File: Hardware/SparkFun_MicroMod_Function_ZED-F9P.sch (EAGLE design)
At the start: 107 parts, among them J1 USB Female Type C Connector, J10 U.FL, J11 455-1750-1-ND, J15 QWIIC_RA, J16 QWIIC_RA, J18 Bus Selection, J2 MICROMOD_STANDARD, J3 Bus Selection, Q1 DMP21D0UT, U1 SN74LVC1G66DRYR, U10 SN74AUP1T04DCK, U11 SN74AUP1T04DCK, U2 3.3V, U3 EEPROM, U4 74LVC4066D_QUAD_BILATERAL_SWI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, U5 74LVC4066D_QUAD_BILATERAL_SWI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, U6 OPA344, U7 74LVC541ABQ, U8 U-BLOX_ZED-F9P, U9 FIN1017MXSOIC-8

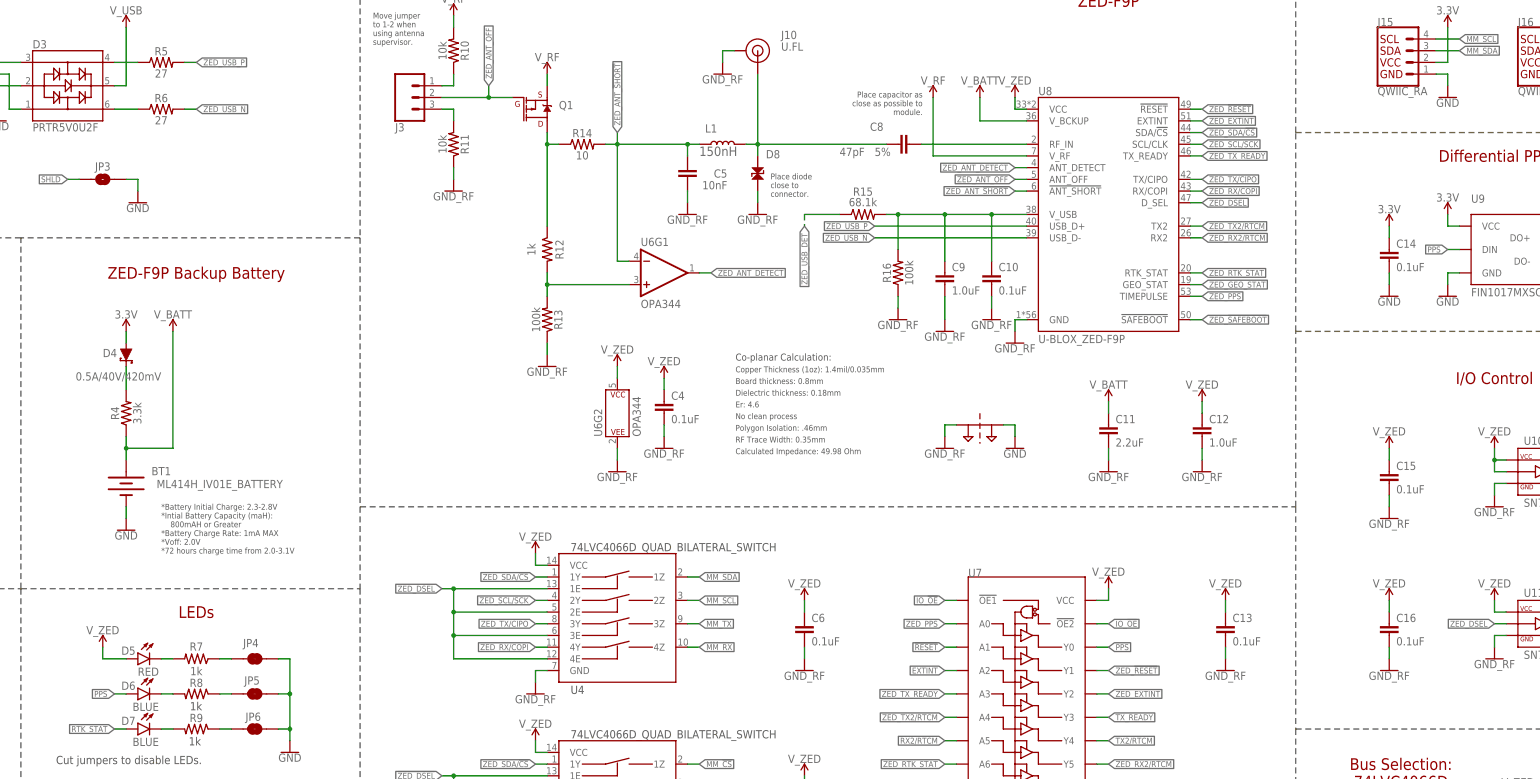
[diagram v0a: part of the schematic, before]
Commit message: Everything tentatively placed on board.
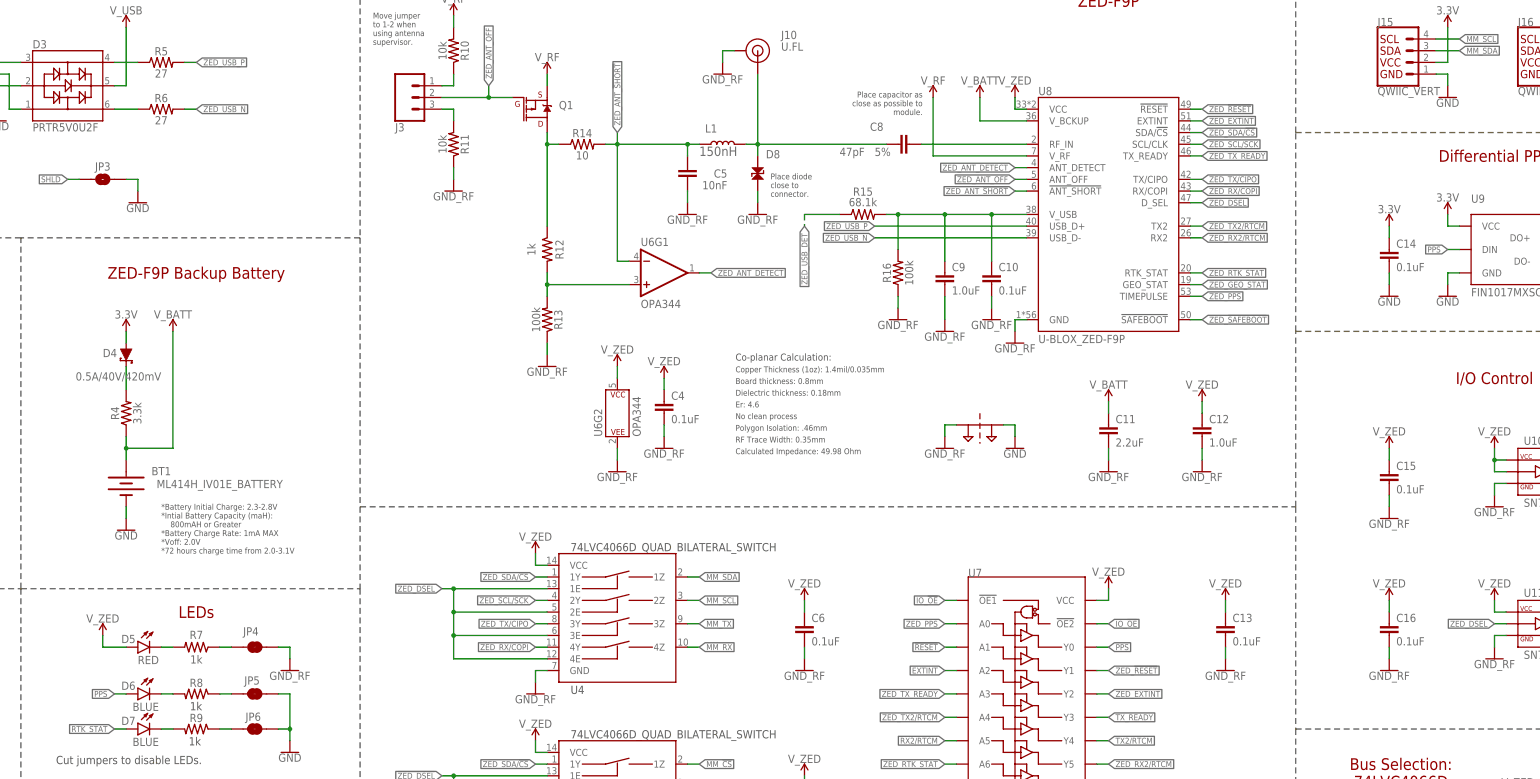
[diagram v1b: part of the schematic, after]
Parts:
- J15: value QWIIC_RA -> QWIIC_VERT; device SparkFun-Connectors:QWIIC_CONNECTORJS-1MM -> SparkFun-Connectors:QWIIC_CONNECTOR
- J7: device SparkFun-Connectors:CONN_01 -> SparkFun-Connectors:CONN_01PTH_NO_SILK_SMALL
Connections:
- net GND: no longer JP4.2
- net GND_RF: now also JP4.2
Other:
- moved on the sheet: D5, JP4, R7

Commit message: 1st draft power planes.
Added split power planes to layout on inner layers.
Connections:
- net N$51 renamed PPS_DIFF_N
- net N$9 renamed PPS_DIFF_P
- net GND: no longer U1.VSS
- net GND_RF: now also U1.VSS

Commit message: Board updates from time off.
Airport board layout was time well spent.
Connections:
- net N$1 renamed USBC_P
- net N$2 renamed USBC_N
- net N$5 renamed USB_P
- net N$6 renamed USB_N
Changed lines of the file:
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@@
 <clearance class="1" value="0.64"/>
 <clearance class="2" value="0.46"/>
+<clearance class="3" value="0.1"/>
 </class>
-<class number="4" name="3.3V" width="0" drill="0">
+<class number="4" name="3.3V" width="0.2" drill="0">
+<clearance class="1" value="0.2"/>
 </class>
 <class number="5" name="5V" width="0" drill="0">
+<clearance class="1" value="0.2"/>
 <clearance class="4" value="0.1"/>
 </class>
-<class number="6" name="USB_DIFF" width="0" drill="0">
+<class number="6" name="USB_DIFF" width="0.2" drill="0">
 </class>
 <class number="7" name="V_ZED" width="0" drill="0">
+<clearance class="1" value="0.2"/>
+<clearance class="2" value="0.2"/>
 <clearance class="4" value="0.64"/>
 </class>
-<class number="8" name="V_RF" width="0.35" drill="0">
+<class number="8" name="V_RF" width="0.2" drill="0">
 <clearance class="2" value="0.46"/>
 </class>
-<class number="9" name="PPS_DIFF" width="0" drill="0">
+<class number="9" name="PPS_DIFF" width="0.2" drill="0">
 </class>
-<class number="10" name="DIGITAL" width="0" drill="0">
+<class number="10" name="DIGITAL" width="0.09" drill="0">
+<clearance class="0" value="0.1"/>
+<clearance class="1" value="0.1"/>
+<clearance class="10" value="0.1"/>
 </class>
-<class number="11" name="ZED_DIG" width="0" drill="0">
+<class number="11" name="ZED_DIG" width="0.1" drill="0">
+<clearance class="0" value="0.2"/>
+<clearance class="1" value="0.2"/>
+<clearance class="2" value="0.2"/>
+<clearance class="3" value="0.46"/>
+<clearance class="7" value="0.1"/>
+<clearance class="11" value="0.1"/>
 </class>
 </classes>
@@
 </segment>
 </net>
-<net name="N$1" class="0">
+<net name="USBC_P" class="6">
 <segment>
 <wire x1="40.64" y1="248.92" x2="73.66" y2="248.92" width="0.1524" layer="91"/>
@@
 </segment>
 </net>
-<net name="N$2" class="0">
+<net name="USBC_N" class="6">
 <segment>
 <wire x1="40.64" y1="246.38" x2="71.12" y2="246.38" width="0.1524" layer="91"/>
@@
 </segment>
 </net>
-<net name="N$5" class="0">
+<net name="USB_P" class="6">
 <segment>
 <pinref part="R5" gate="G$1" pin="1"/>
@@
 </segment>
 </net>
-<net name="N$6" class="0">
+<net name="USB_N" class="6">
 <segment>
 <pinref part="R6" gate="G$1" pin="1"/>
@@
 </segment>
 </net>
-<net name="N$14" class="5">
+<net name="N$14" class="4">
 <segment>
 <pinref part="R15" gate="&gt;NAME" pin="2"/>

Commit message: Update sch after fixing lib.
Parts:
- JP3: value JUMPER-SMT_2_NO_SILK -> JUMPER-SMT_2_NC_TRACE_SILK; device SparkFun-Jumpers:JUMPER-SMT_2_NO_SILK -> SparkFun-Jumpers:JUMPER-SMT_2_NC_TRACE_SILK
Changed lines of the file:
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@@
 </class>
 <class number="7" name="V_ZED" width="0" drill="0">
-<clearance class="1" value="0.2"/>
+<clearance class="1" value="0.64"/>
 <clearance class="2" value="0.2"/>
 <clearance class="4" value="0.64"/>
@@
 <part name="SUPPLY28" library="SparkFun-PowerSymbols" deviceset="3.3V" device=""/>
 <part name="SUPPLY29" library="SparkFun-PowerSymbols" deviceset="3.3V" device=""/>
-<part name="JP3" library="SparkFun-Jumpers" deviceset="JUMPER-SMT_2_NO" device="_SILK" package3d_urn="urn:adsk.eagle:package:39279/1"/>
+<part name="JP3" library="SparkFun-Jumpers" deviceset="JUMPER-SMT_2_NC_TRACE" device="_SILK" package3d_urn="urn:adsk.eagle:package:39281/1"/>
 <part name="GND5" library="SparkFun-PowerSymbols" deviceset="GND" device=""/>
 <part name="JP1" library="SparkFun-Jumpers" deviceset="JUMPER-SMT_2_NO" device="_SILK" package3d_urn="urn:adsk.eagle:package:39279/1"/>

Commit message: Replace backup battery.
New part now in use.
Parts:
- BT1: value ML414H_IV01E_BATTERY -> RELOWABLE_BATTERY_MS421R; device SparkFun-Batteries:ML414H_IV01E_BATTERY -> SparkFun-Batteries:RELOWABLE_BATTERY_MS421R
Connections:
- net GEO_STAT: now also J2.F6; no longer J2.F5
- net RTK_STAT: now also J2.F5; no longer J2.F6
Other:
- note added: "*Battery Initial Charge: 2.8-3.3V *Intial Battery Capacity (maH): 1.5mAh *Battery Charge Rate: 1mA MAX *Voff: 2.0V *120 hours charge time from 2.0-3.1V"
- note removed: "*Battery Initial Charge: 2.3-2.8V *Intial Battery Capacity (maH): 800mAH or Greater *Battery Charge Rate: 1mA MAX *Voff: 2.0V *72 hours charge time from 2.0-3.1V"
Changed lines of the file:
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@@
 <part name="SUPPLY11" library="SparkFun-PowerSymbols" deviceset="3.3V" device=""/>
 <part name="D4" library="SparkFun-DiscreteSemi" deviceset="DIODE-SCHOTTKY" device="-PMEG4005EJ" value="0.5A/40V/420mV"/>
-<part name="BT1" library="SparkFun-Batteries" deviceset="ML414H_IV01E_BATTERY" device=""/>
+<part name="BT1" library="SparkFun-Batteries" deviceset="RELOWABLE_BATTERY" device="_MS421R"/>
 <part name="D6" library="SparkFun-LED" deviceset="LED-BLUE" device="0603" value="BLUE"/>
 <part name="D7" library="SparkFun-LED" deviceset="LED-BLUE" device="0603" value="BLUE"/>
@@
 <text x="228.854" y="184.15" size="1.524" layer="97" font="vector" ratio="15">Co-planar Calculation:</text>
 <text x="228.854" y="163.83" size="1.27" layer="97" font="vector">Calculated Impedance: 49.98 Ohm</text>
-<text x="104.14" y="142.24" size="1.27" layer="97" font="vector">*Battery Initial Charge: 2.3-2.8V
+<text x="104.14" y="142.24" size="1.27" layer="97" font="vector">*Battery Initial Charge: 2.8-3.3V
 *Intial Battery Capacity (maH):
-    800mAH or Greater
+    1.5mAh
 *Battery Charge Rate: 1mA MAX
 *Voff: 2.0V
-*72 hours charge time from 2.0-3.1V</text>
+*120 hours charge time from 2.0-3.1V</text>
 <text x="269.494" y="237.49" size="1.27" layer="97" font="vector" align="bottom-right">Place capacitor as
 close as possible to
@@
 <instance part="BT1" gate="G$1" x="96.52" y="157.48" smashed="yes" rot="R270">
 <attribute name="NAME" x="104.14" y="159.258" size="1.778" layer="95" font="vector" align="bottom-center"/>
-<attribute name="VALUE" x="116.84" y="158.242" size="1.778" layer="96" font="vector" align="top-center"/>
 </instance>
 <instance part="D6" gate="G$1" x="99.06" y="111.76" smashed="yes" rot="MR270">
@@
 </segment>
 <segment>
-<wire x1="116.84" y1="17.78" x2="114.3" y2="17.78" width="0.1524" layer="91"/>
-<label x="116.84" y="17.78" size="1.27" layer="95" xref="yes"/>
-<pinref part="J2" gate="J1" pin="F6"/>
+<wire x1="116.84" y1="20.32" x2="114.3" y2="20.32" width="0.1524" layer="91"/>
+<pinref part="J2" gate="J1" pin="F5"/>
+<label x="116.84" y="20.32" size="1.27" layer="95" xref="yes"/>
 </segment>
 </net>
@@
 </segment>
 <segment>
-<wire x1="116.84" y1="20.32" x2="114.3" y2="20.32" width="0.1524" layer="91"/>
-<label x="116.84" y="20.32" size="1.27" layer="95" xref="yes"/>
-<pinref part="J2" gate="J1" pin="F5"/>
-</segment>
-</net>
+<wire x1="116.84" y1="17.78" x2="114.3" y2="17.78" width="0.1524" layer="91"/>
+<pinref part="J2" gate="J1" pin="F6"/>
+<label x="116.84" y="17.78" size="1.27" layer="95" xref="yes"/>
+</segment>
+</net>

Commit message: Change net class for vbatt.
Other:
- note added: "*Battery Initial Charge: 2.8-3.3V *Intial Battery Capacity (maH): 1.5mAh *Battery Charge Rate: 0.03mA MAX *Voff: 2.0V *120 hours charge time from 2.0-3.1V"
- note removed: "*Battery Initial Charge: 2.8-3.3V *Intial Battery Capacity (maH): 1.5mAh *Battery Charge Rate: 1mA MAX *Voff: 2.0V *120 hours charge time from 2.0-3.1V"
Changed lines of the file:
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@@
 <clearance class="2" value="0.2"/>
 <clearance class="4" value="0.64"/>
+<clearance class="5" value="0.2"/>
 </class>
 <class number="8" name="V_RF" width="0.2" drill="0">
@@
 *Intial Battery Capacity (maH):
     1.5mAh
-*Battery Charge Rate: 1mA MAX
+*Battery Charge Rate: 0.03mA MAX
 *Voff: 2.0V
 *120 hours charge time from 2.0-3.1V</text>
@@
 </segment>
 </net>
-<net name="V_BATT" class="4">
+<net name="V_BATT" class="5">
 <segment>
 <wire x1="96.52" y1="162.56" x2="96.52" y2="165.1" width="0.1524" layer="91"/>

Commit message: Silks complete.
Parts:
- removed LOGO1: SFE_LOGO_NAME_FLAME.1_INCH, SparkFun-Aesthetics:SFE_LOGO_NAME_FLAME.1_INCH
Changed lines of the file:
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@@
 <part name="FD4" library="SparkFun-Aesthetics" deviceset="FIDUCIAL" device="UFIDUCIAL"/>
 <part name="FD2" library="SparkFun-Aesthetics" deviceset="FIDUCIAL" device="UFIDUCIAL"/>
-<part name="LOGO1" library="SparkFun-Aesthetics" deviceset="SFE_LOGO_NAME_FLAME" device=".1_INCH"/>
 <part name="LOGO3" library="SparkFun-Aesthetics" deviceset="OSHW-LOGO" device="MINI"/>
 <part name="J2" library="SparkFun-MicroMod-Function" deviceset="MICROMOD" device="_STANDARD"/>
@@
 <instance part="FD4" gate="G$1" x="429.26" y="27.94" smashed="yes"/>
 <instance part="FD2" gate="G$1" x="426.72" y="27.94" smashed="yes"/>
-<instance part="LOGO1" gate="G$1" x="345.44" y="35.56" smashed="yes"/>
 <instance part="LOGO3" gate="G$1" x="419.1" y="45.72" smashed="yes"/>
 <instance part="J2" gate="J1" x="96.52" y="45.72" smashed="yes">
